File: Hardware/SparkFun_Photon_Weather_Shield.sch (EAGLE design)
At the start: 43 parts, among them U1 3.3V MIC5219, U2 HTU21D, U3 MPL3115A2LGA8

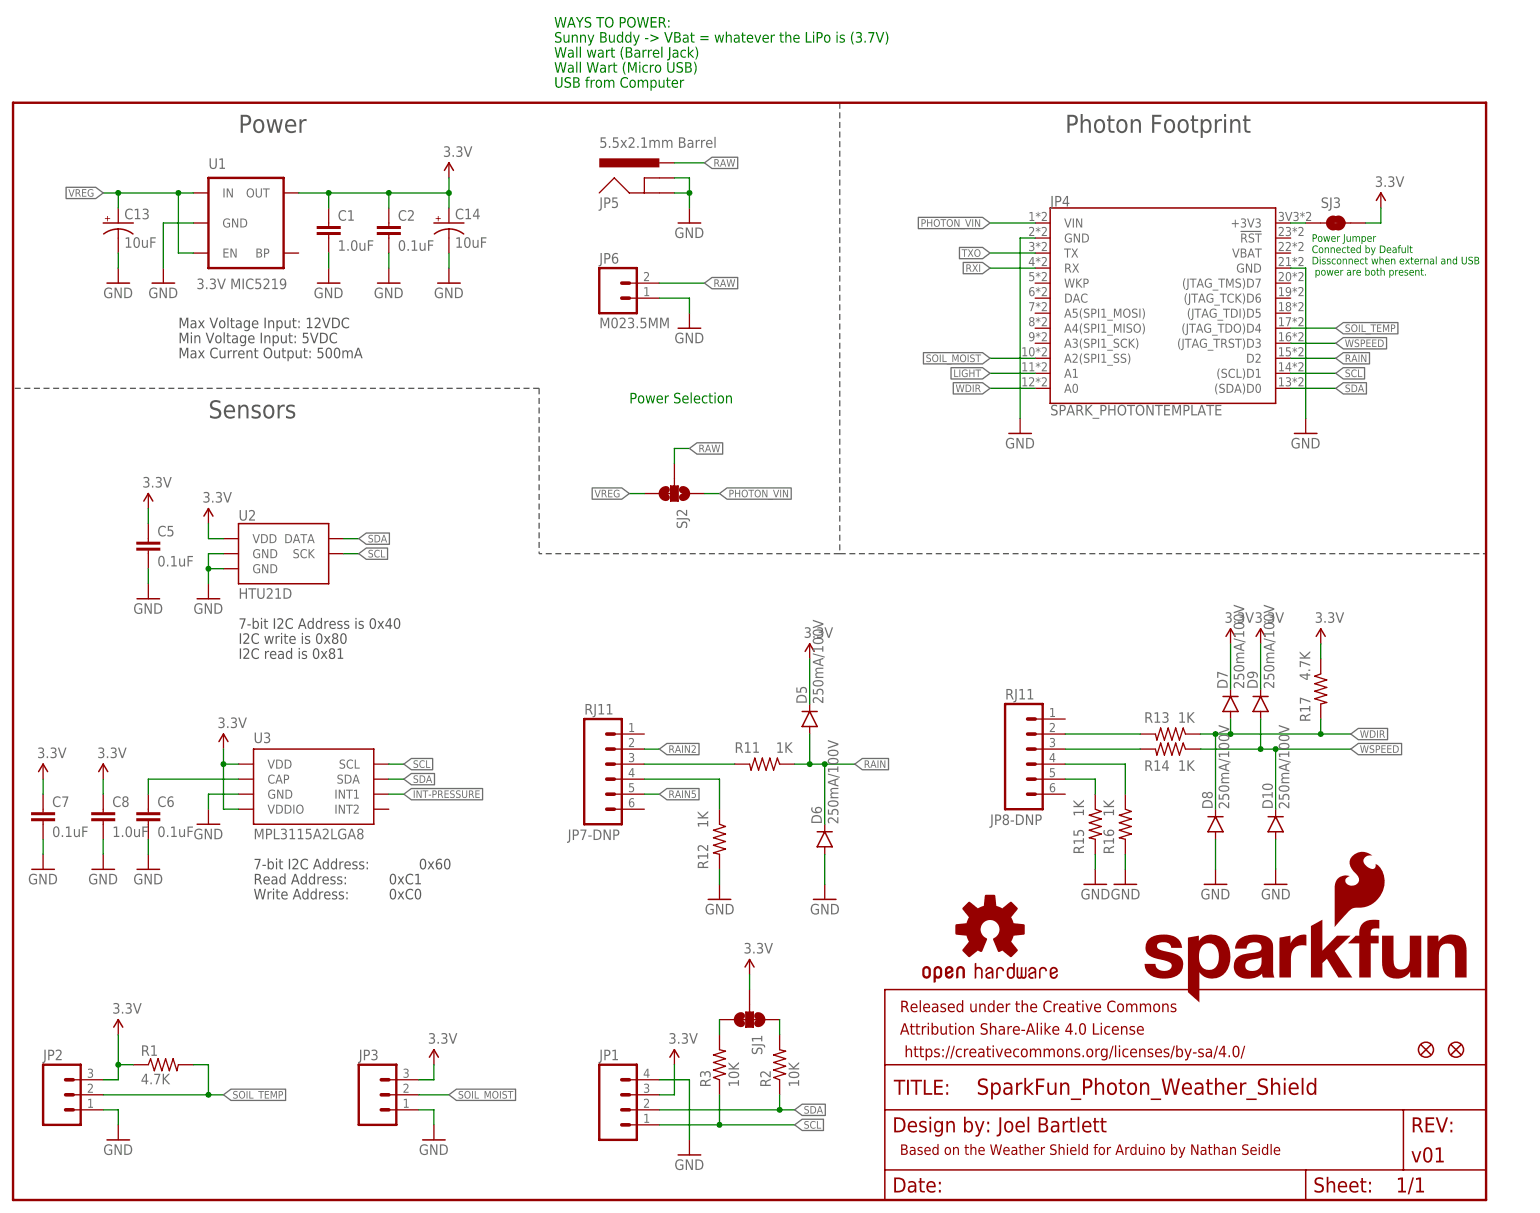
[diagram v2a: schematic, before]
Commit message: QC Checklist Issues Addressed
QC Checklist Issues Addressed: added PROD_IDs to few missing parts,
changed Y junctions to T junctions, fixed pin 1 markings, added Values
where needed.
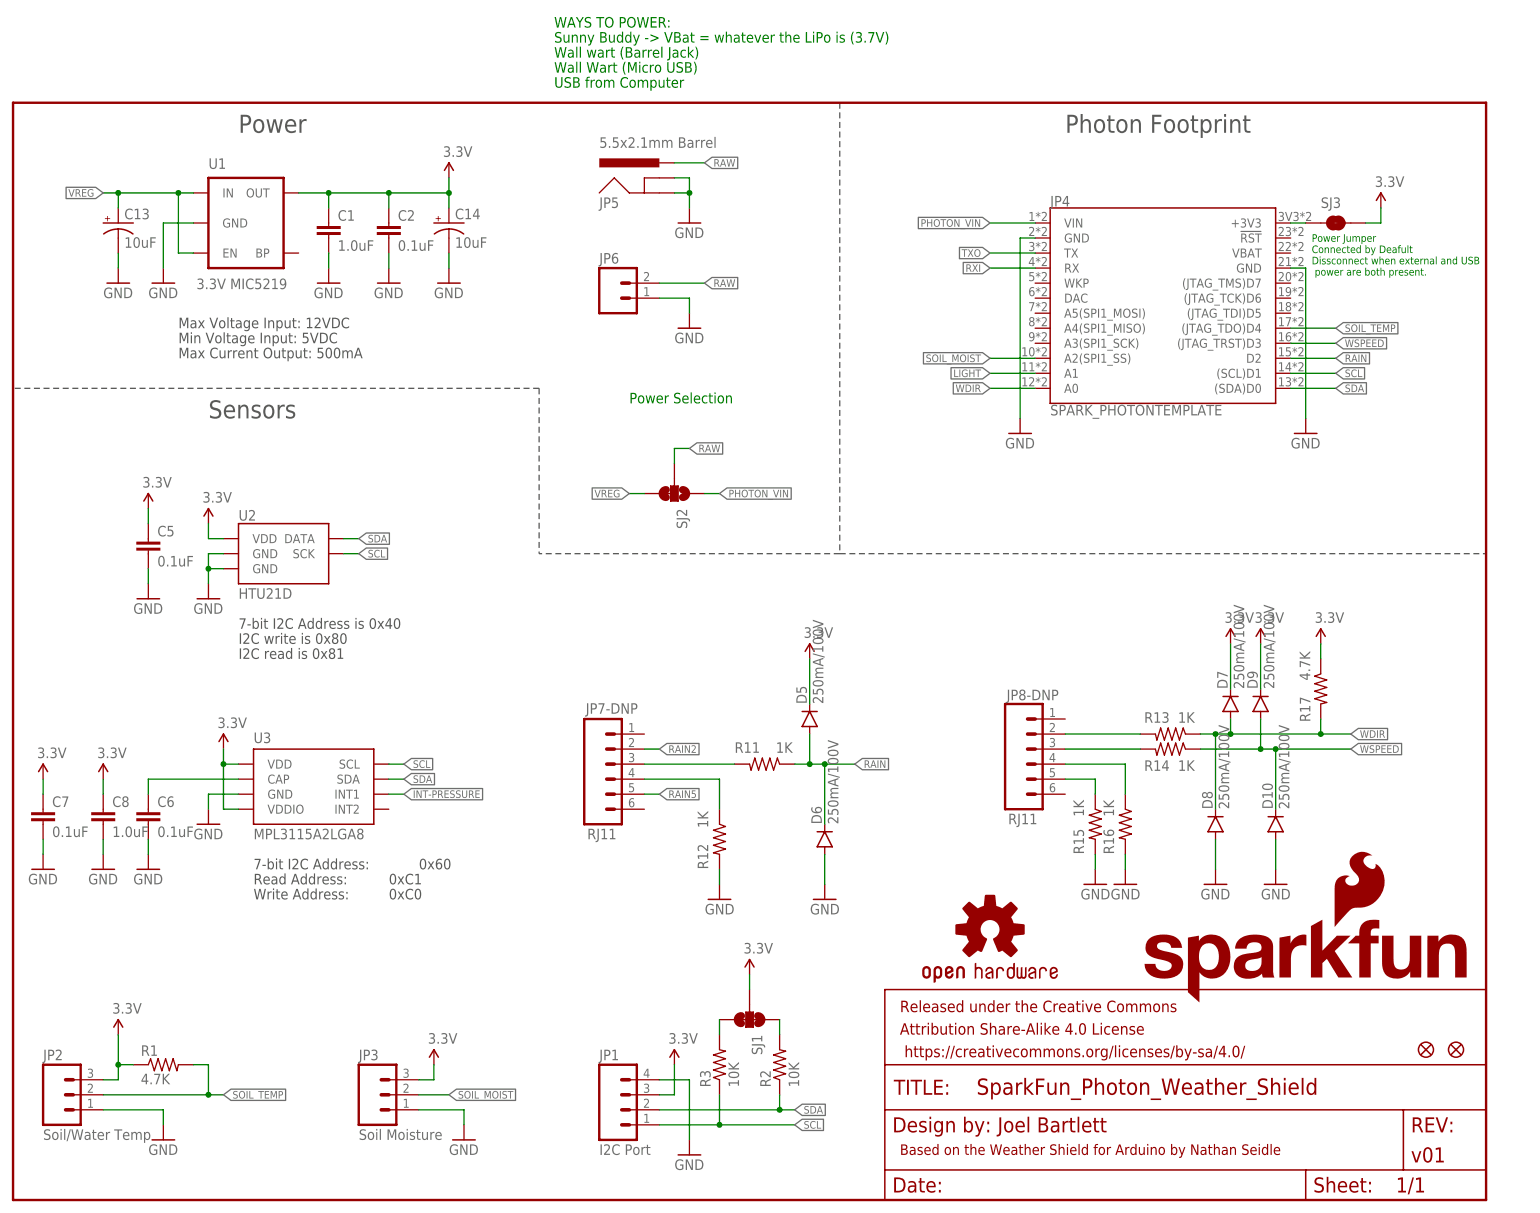
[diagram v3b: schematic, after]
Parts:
- JP1: value (none) -> I2C Port
- JP2: value (none) -> Soil/Water Temp
- JP3: value (none) -> Soil Moisture
- JP6: value M023.5MM -> (none)
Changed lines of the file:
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@@
 <part name="LOGO1" library="SparkFun-Aesthetics" deviceset="OSHW-LOGO" device="M"/>
 <part name="P+2" library="SparkFun" deviceset="3.3V" device=""/>
-<part name="JP2" library="SparkFun-Connectors" deviceset="M03" device="PTH"/>
-<part name="JP3" library="SparkFun-Connectors" deviceset="M03" device="PTH"/>
+<part name="JP2" library="SparkFun-Connectors" deviceset="M03" device="PTH" value="Soil/Water Temp"/>
+<part name="JP3" library="SparkFun-Connectors" deviceset="M03" device="PTH" value="Soil Moisture"/>
 <part name="GND3" library="SparkFun" deviceset="GND" device=""/>
 <part name="R1" library="SparkFun-Resistors" deviceset="4.7KOHM-1/10W-1%(0603)" device="" value="4.7K"/>
 <part name="GND4" library="SparkFun" deviceset="GND" device=""/>
 <part name="JP4" library="template_temp" deviceset="SPARK_PHOTON" device="TEMPLATE"/>
-<part name="JP1" library="SparkFun-Connectors" deviceset="M04" device="PTH"/>
+<part name="JP1" library="SparkFun-Connectors" deviceset="M04" device="PTH" value="I2C Port"/>
 <part name="SJ1" library="SparkFun-Passives" deviceset="JUMPER-PAD-3-NC_BY_TRACE" device=""/>
 <part name="GND8" library="SparkFun" deviceset="GND" device=""/>
@@
 </instance>
 <instance part="JP8-DNP" gate="G$1" x="172.72" y="76.2" smashed="yes" rot="MR180">
-<attribute name="NAME" x="165.1" y="63.373" size="1.778" layer="95"/>
-<attribute name="VALUE" x="167.64" y="86.36" size="1.778" layer="96" rot="MR180"/>
+<attribute name="NAME" x="167.894" y="84.455" size="1.778" layer="95"/>
+<attribute name="VALUE" x="168.148" y="65.278" size="1.778" layer="96" rot="MR180"/>
 </instance>
 <instance part="JP7-DNP" gate="G$1" x="101.6" y="73.66" smashed="yes" rot="MR180">
-<attribute name="NAME" x="93.726" y="60.833" size="1.778" layer="95"/>
-<attribute name="VALUE" x="96.52" y="83.82" size="1.778" layer="96" rot="MR180"/>
+<attribute name="NAME" x="96.774" y="82.169" size="1.778" layer="95"/>
+<attribute name="VALUE" x="97.028" y="62.738" size="1.778" layer="96" rot="MR180"/>
 </instance>
 <instance part="GND5" gate="1" x="119.38" y="50.8" rot="MR0"/>
@@
 <instance part="JP2" gate="G$1" x="7.62" y="17.78"/>
 <instance part="JP3" gate="G$1" x="60.96" y="17.78"/>
-<instance part="GND3" gate="1" x="17.78" y="10.16"/>
+<instance part="GND3" gate="1" x="25.4" y="10.16"/>
 <instance part="R1" gate="G$1" x="25.4" y="22.86"/>
-<instance part="GND4" gate="1" x="71.12" y="10.16"/>
+<instance part="GND4" gate="1" x="76.2" y="10.16"/>
 <instance part="JP4" gate="G$1" x="195.58" y="149.86"/>
 <instance part="JP1" gate="G$1" x="104.14" y="15.24"/>
@@
 <pinref part="JP2" gate="G$1" pin="1"/>
 <pinref part="GND3" gate="1" pin="GND"/>
-<wire x1="15.24" y1="15.24" x2="17.78" y2="15.24" width="0.1524" layer="91"/>
-<wire x1="17.78" y1="15.24" x2="17.78" y2="12.7" width="0.1524" layer="91"/>
+<wire x1="15.24" y1="15.24" x2="25.4" y2="15.24" width="0.1524" layer="91"/>
+<wire x1="25.4" y1="15.24" x2="25.4" y2="12.7" width="0.1524" layer="91"/>
 </segment>
 <segment>
 <pinref part="JP3" gate="G$1" pin="1"/>
 <pinref part="GND4" gate="1" pin="GND"/>
-<wire x1="68.58" y1="15.24" x2="71.12" y2="15.24" width="0.1524" layer="91"/>
-<wire x1="71.12" y1="15.24" x2="71.12" y2="12.7" width="0.1524" layer="91"/>
-</segment>
-<segment>
+<wire x1="68.58" y1="15.24" x2="76.2" y2="15.24" width="0.1524" layer="91"/>
+<wire x1="76.2" y1="15.24" x2="76.2" y2="12.7" width="0.1524" layer="91"/>
+</segment>
+<segment>

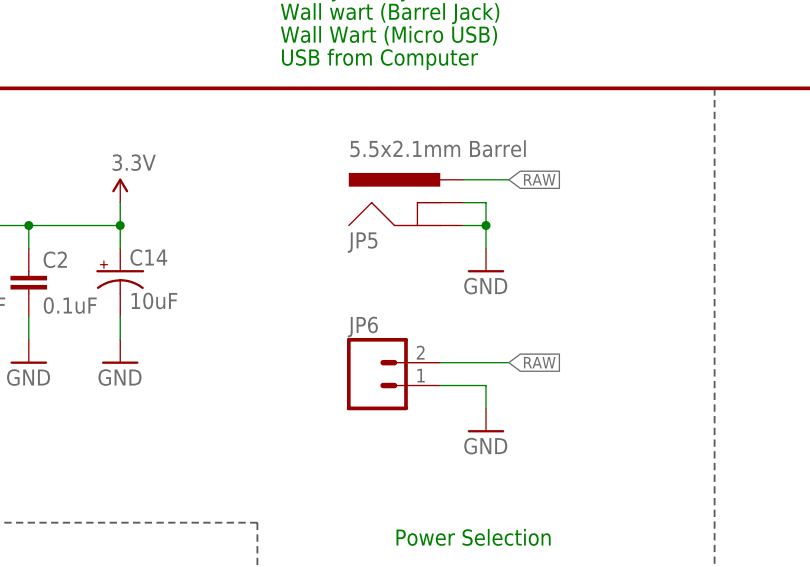
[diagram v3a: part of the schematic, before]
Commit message: Added DNP to a few connectors
Added DNP to a few connectors that I missed and do not need to be
populated.
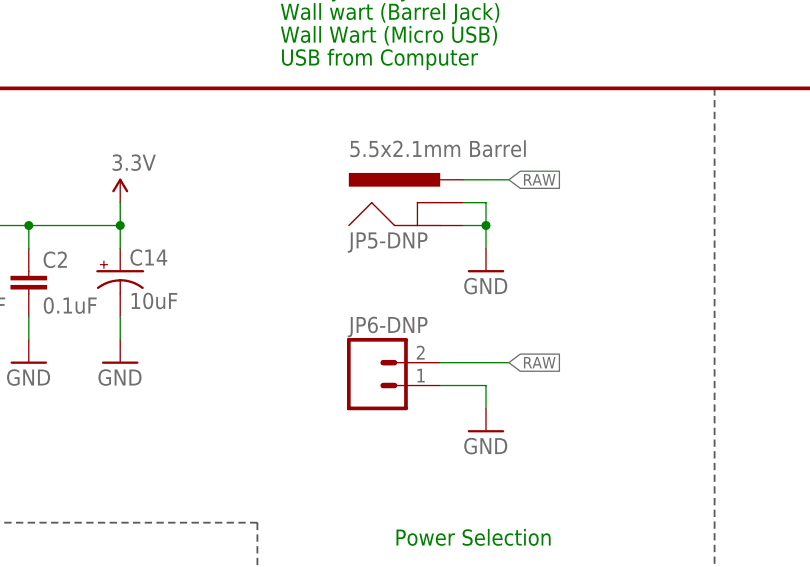
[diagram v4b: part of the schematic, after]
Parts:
- renumbered JP5 to JP5-DNP, JP6 to JP6-DNP
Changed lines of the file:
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@@
 <part name="R2" library="SparkFun-Resistors" deviceset="10KOHM-1/10W-1%(0603)" device="0603" value="10K"/>
 <part name="R3" library="SparkFun-Resistors" deviceset="10KOHM-1/10W-1%(0603)" device="0603" value="10K"/>
-<part name="JP5" library="SparkFun-Connectors" deviceset="POWER_JACK" device="SMD" value="5.5x2.1mm Barrel"/>
-<part name="JP6" library="SparkFun-Connectors" deviceset="M02" device="3.5MM"/>
+<part name="JP5-DNP" library="SparkFun-Connectors" deviceset="POWER_JACK" device="SMD" value="5.5x2.1mm Barrel"/>
+<part name="JP6-DNP" library="SparkFun-Connectors" deviceset="M02" device="3.5MM"/>
 <part name="P+5" library="SparkFun" deviceset="VCC" device="" value="3.3V"/>
 <part name="P+11" library="SparkFun" deviceset="VCC" device="" value="3.3V"/>
@@
 <instance part="R2" gate="G$1" x="129.54" y="22.86" rot="R90"/>
 <instance part="R3" gate="G$1" x="119.38" y="22.86" rot="R90"/>
-<instance part="JP5" gate="G$1" x="109.22" y="167.64"/>
-<instance part="JP6" gate="G$1" x="101.6" y="152.4"/>
+<instance part="JP5-DNP" gate="G$1" x="109.22" y="167.64"/>
+<instance part="JP6-DNP" gate="G$1" x="101.6" y="152.4"/>
 <instance part="P+5" gate="1" x="134.62" y="91.44"/>
 <instance part="P+11" gate="1" x="205.74" y="93.98"/>
@@
 </segment>
 <segment>
-<pinref part="JP5" gate="G$1" pin="GNDBREAK"/>
+<pinref part="JP5-DNP" gate="G$1" pin="GNDBREAK"/>
 <pinref part="GND10" gate="1" pin="GND"/>
 <wire x1="111.76" y1="172.72" x2="114.3" y2="172.72" width="0.1524" layer="91"/>
 <wire x1="114.3" y1="172.72" x2="114.3" y2="170.18" width="0.1524" layer="91"/>
-<pinref part="JP5" gate="G$1" pin="GND"/>
+<pinref part="JP5-DNP" gate="G$1" pin="GND"/>
 <wire x1="114.3" y1="170.18" x2="114.3" y2="167.64" width="0.1524" layer="91"/>
 <wire x1="111.76" y1="170.18" x2="114.3" y2="170.18" width="0.1524" layer="91"/>
@@
 </segment>
 <segment>
-<pinref part="JP6" gate="G$1" pin="1"/>
+<pinref part="JP6-DNP" gate="G$1" pin="1"/>
 <wire x1="109.22" y1="152.4" x2="114.3" y2="152.4" width="0.1524" layer="91"/>
 <wire x1="114.3" y1="152.4" x2="114.3" y2="149.86" width="0.1524" layer="91"/>
@@
 <net name="RAW" class="1">
 <segment>
-<pinref part="JP5" gate="G$1" pin="PWR"/>
+<pinref part="JP5-DNP" gate="G$1" pin="PWR"/>
 <wire x1="111.76" y1="175.26" x2="116.84" y2="175.26" width="0.1524" layer="91"/>
 <label x="116.84" y="175.26" size="1.27" layer="95" xref="yes"/>
 </segment>
 <segment>
-<pinref part="JP6" gate="G$1" pin="2"/>
+<pinref part="JP6-DNP" gate="G$1" pin="2"/>
 <wire x1="109.22" y1="154.94" x2="116.84" y2="154.94" width="0.1524" layer="91"/>
 <label x="116.84" y="154.94" size="1.27" layer="95" xref="yes"/>

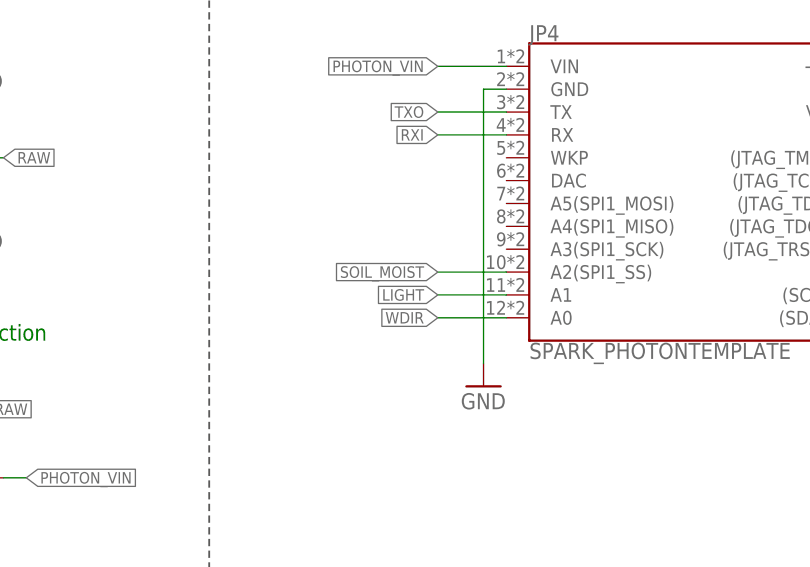
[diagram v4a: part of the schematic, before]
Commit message: Ready for Protos
Moved Soil_Moisture from A2 to A1 and deleted unused Light  net on A1.
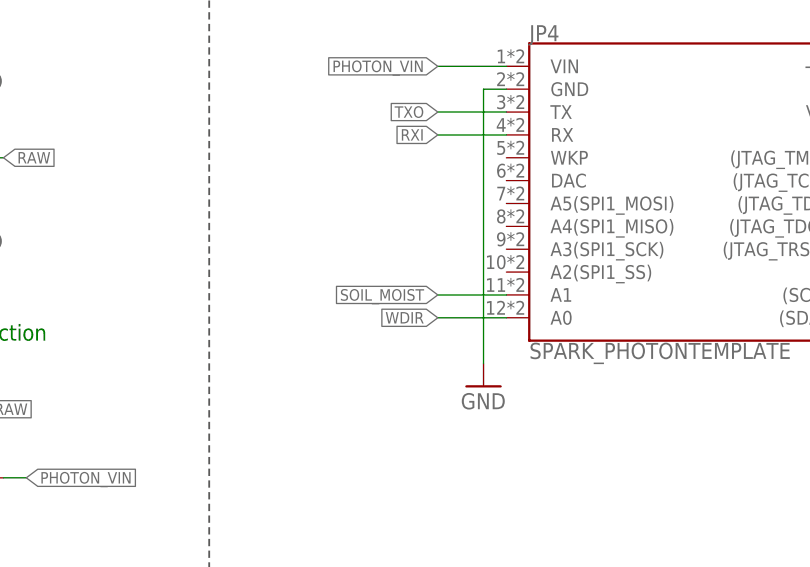
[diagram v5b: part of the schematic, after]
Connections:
- removed net LIGHT: JP4.A1
- net SOIL_MOIST: now also JP4.A1; no longer JP4.A2(SPI1_SS)
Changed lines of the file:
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@@
-</segment>
-</net>
-<net name="LIGHT" class="0">
-<segment>
-<wire x1="172.72" y1="139.7" x2="165.1" y2="139.7" width="0.1524" layer="91"/>
-<label x="165.1" y="139.7" size="1.27" layer="95" rot="R180" xref="yes"/>
-<pinref part="JP4" gate="G$1" pin="A1"/>
 </segment>
 </net>
@@
 <net name="SOIL_MOIST" class="0">
 <segment>
-<wire x1="172.72" y1="142.24" x2="165.1" y2="142.24" width="0.1524" layer="91"/>
-<label x="165.1" y="142.24" size="1.27" layer="95" rot="R180" xref="yes"/>
-<pinref part="JP4" gate="G$1" pin="A2(SPI1_SS)"/>
-</segment>
-<segment>
 <pinref part="JP3" gate="G$1" pin="2"/>
 <wire x1="68.58" y1="17.78" x2="73.66" y2="17.78" width="0.1524" layer="91"/>
 <label x="73.66" y="17.78" size="1.27" layer="95" xref="yes"/>
 </segment>
+<segment>
+<pinref part="JP4" gate="G$1" pin="A1"/>
+<wire x1="172.72" y1="139.7" x2="165.1" y2="139.7" width="0.1524" layer="91"/>
+<label x="165.1" y="139.7" size="1.27" layer="95" rot="R180" xref="yes"/>
+</segment>
 </net>
